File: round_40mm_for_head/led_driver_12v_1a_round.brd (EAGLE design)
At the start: 38 x 38 mm, 44 parts, among them IC1 LM2936MP-3.0, Q1 BSZ0902NSI, Q2 BSZ0902NSI, Q3 BSZ0902NSI, Q4 BSZ0902NSI, Q5 BSZ0902NSI, X1 87758-1016

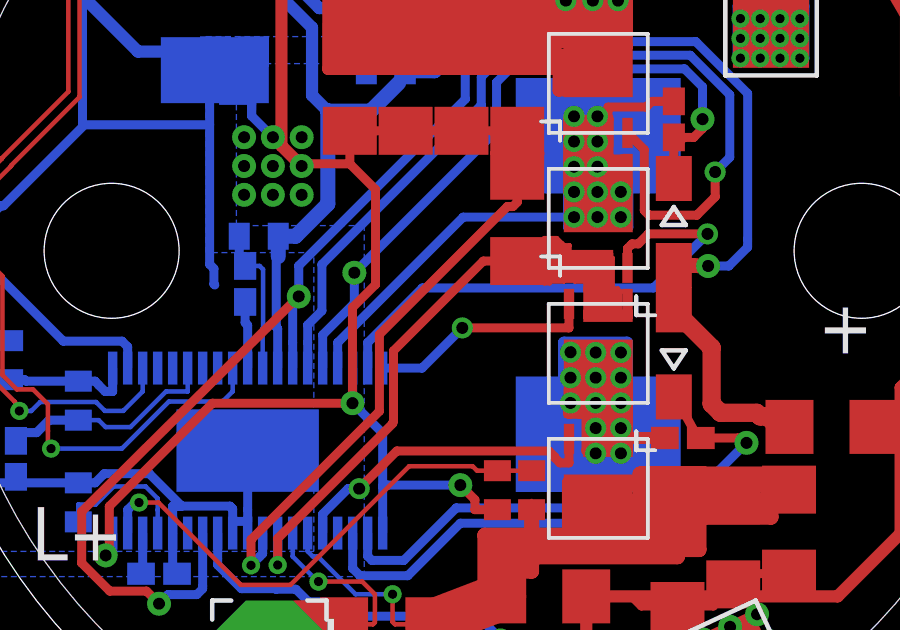
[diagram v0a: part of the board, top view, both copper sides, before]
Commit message: kevlin connection changed
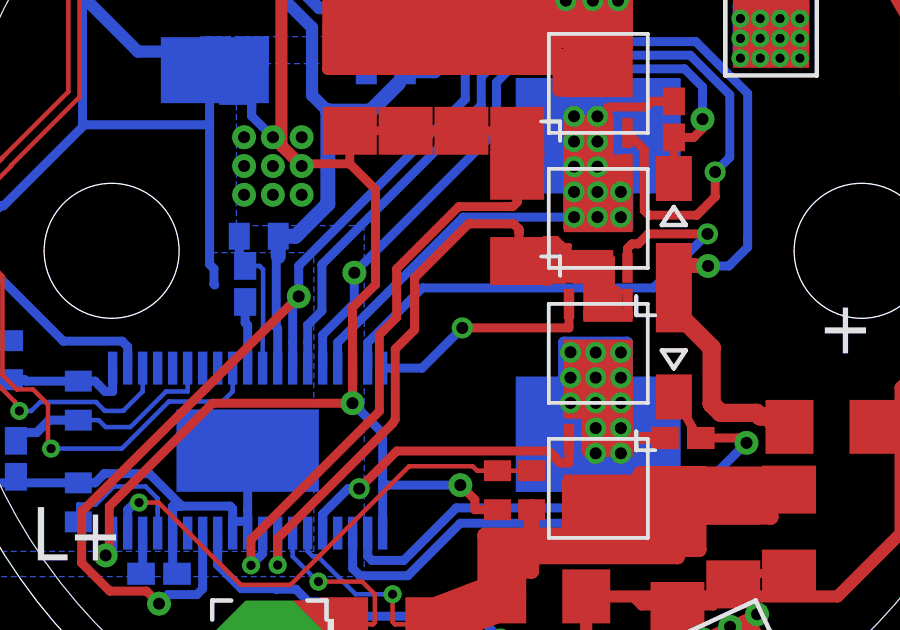
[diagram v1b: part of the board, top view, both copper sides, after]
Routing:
- net SNSP: track 58.4 -> 61.2 mm
- net SNSN: track 18.0 -> 19.0 mm
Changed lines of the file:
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@@
 <element name="PAD4" library="wirepad" package="5-2,5" value="LED+" x="25.08" y="3.78" smashed="yes" rot="R115"/>
 <element name="U$4" library="SparkFun-Passives" package="GND_CONNECT" value="GND_CONNECT" x="8.955" y="23.625" smashed="yes" rot="MR270"/>
-<element name="IC1" library="national-semiconductor" package="SOT223" value="LM2936MP-3.0" x="8.94" y="27.12" rot="MR180">
+<element name="IC1" library="national-semiconductor" package="SOT223" value="LM2936MP-3.0" x="8.94" y="27.12" smashed="yes" rot="MR180">
 <attribute name="OC_FARNELL" value="1496125" x="8.94" y="27.12" size="1.778" layer="28" rot="MR180" display="off"/>
 <attribute name="MF" value="NATIONAL SEMICONDUCTOR" x="8.94" y="27.12" size="1.778" layer="28" rot="MR180" display="off"/>
@@
 <wire x1="19.02" y1="19.62" x2="18.873390625" y2="19.473390625" width="0.3" layer="1"/>
 <wire x1="18.873390625" y1="19.473390625" x2="18.688" y2="19.473390625" width="0.3" layer="1"/>
-<wire x1="18.688" y1="19.473390625" x2="14.42515" y2="15.210540625" width="0.3" layer="1"/>
+<wire x1="18.688" y1="19.473390625" x2="17.073390625" y2="19.473390625" width="0.3" layer="1"/>
+<wire x1="17.073390625" y1="19.473390625" x2="15" y2="17.4" width="0.3" layer="1"/>
+<wire x1="15" y1="17.4" x2="15" y2="15.78" width="0.3" layer="1"/>
+<wire x1="15" y1="15.78" x2="14.52" y2="15.3" width="0.3" layer="1"/>
+<wire x1="14.52" y1="15.3" x2="14.42515" y2="15.210540625" width="0.3" layer="1"/>
 <wire x1="14.42515" y1="15.210540625" x2="14.42515" y2="12.65243125" width="0.3" layer="1"/>
 <wire x1="14.42515" y1="12.65243125" x2="10.146590625" y2="8.37386875" width="0.3" layer="1"/>
@@
 <contactref element="Q3" pad="S@3"/>
 <contactref element="R8" pad="2"/>
-<wire x1="19.02" y1="17.658" x2="17.889890625" y2="17.658" width="0.3" layer="1"/>
-<wire x1="17.889890625" y1="17.658" x2="14.89588125" y2="14.663990625" width="0.3" layer="1"/>
-<wire x1="14.89588125" y1="14.663990625" x2="14.89588125" y2="12.32296875" width="0.3" layer="1"/>
-<wire x1="14.89588125" y1="12.32296875" x2="14.879590625" y2="12.30668125" width="0.1524" layer="1"/>
-<wire x1="14.879590625" y1="12.30668125" x2="14.87223125" y2="12.24668125" width="0.3" layer="1"/>
+<wire x1="14.95588125" y1="14.723990625" x2="14.95588125" y2="12.38296875" width="0.3" layer="1"/>
+<wire x1="14.95588125" y1="12.38296875" x2="14.939590625" y2="12.36668125" width="0.1524" layer="1"/>
+<wire x1="14.939590625" y1="12.36668125" x2="14.87223125" y2="12.24668125" width="0.3" layer="1"/>
 <wire x1="14.87223125" y1="12.24668125" x2="11.035309375" y2="8.409759375" width="0.3" layer="1"/>
 <wire x1="11.035309375" y1="8.409759375" x2="11.035309375" y2="7.52523125" width="0.3" layer="1"/>
@@
 <via x="11.035309375" y="7.52523125" extent="1-16" drill="0.3048" diameter="0.6096"/>
 <wire x1="21.395" y1="17.43" x2="21.395" y2="16.701390625" width="0.1524" layer="1"/>
+<wire x1="19.02" y1="17.658" x2="19.08" y2="17.658" width="0.4064" layer="1"/>
+<wire x1="19.08" y1="17.658" x2="19.08" y2="18.6" width="0.3048" layer="1"/>
+<wire x1="19.08" y1="18.6" x2="19.08" y2="18.72" width="0.3048" layer="1"/>
+<wire x1="19.08" y1="18.72" x2="18.9" y2="18.9" width="0.3048" layer="1"/>
+<wire x1="18.9" y1="18.9" x2="17.4" y2="18.9" width="0.3048" layer="1"/>
+<wire x1="17.4" y1="18.9" x2="15.6" y2="17.1" width="0.3048" layer="1"/>
+<wire x1="15.6" y1="17.1" x2="15.6" y2="15.368109375" width="0.3048" layer="1"/>
+<wire x1="15.6" y1="15.368109375" x2="14.95588125" y2="14.723990625" width="0.3048" layer="1"/>
 </signal>
 <signal name="ISN">

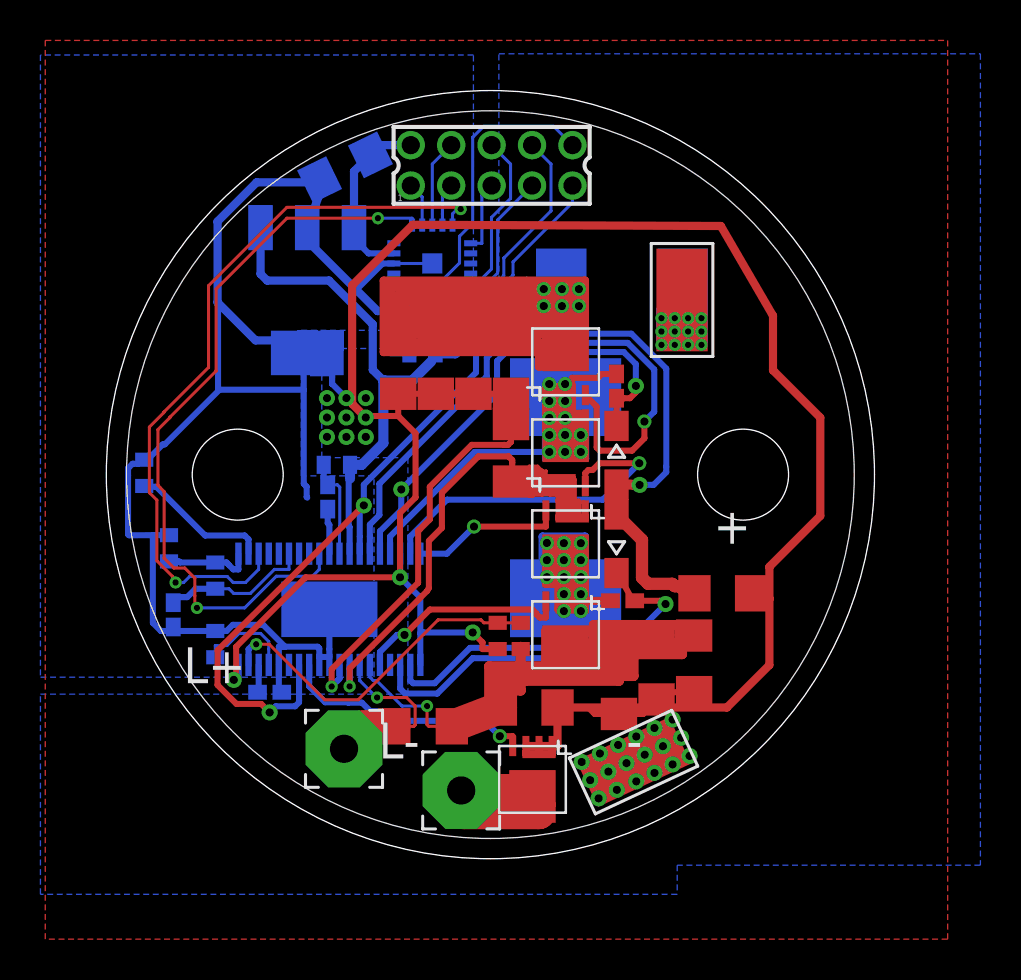
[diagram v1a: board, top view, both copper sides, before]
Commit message: added adc resistors shutdown
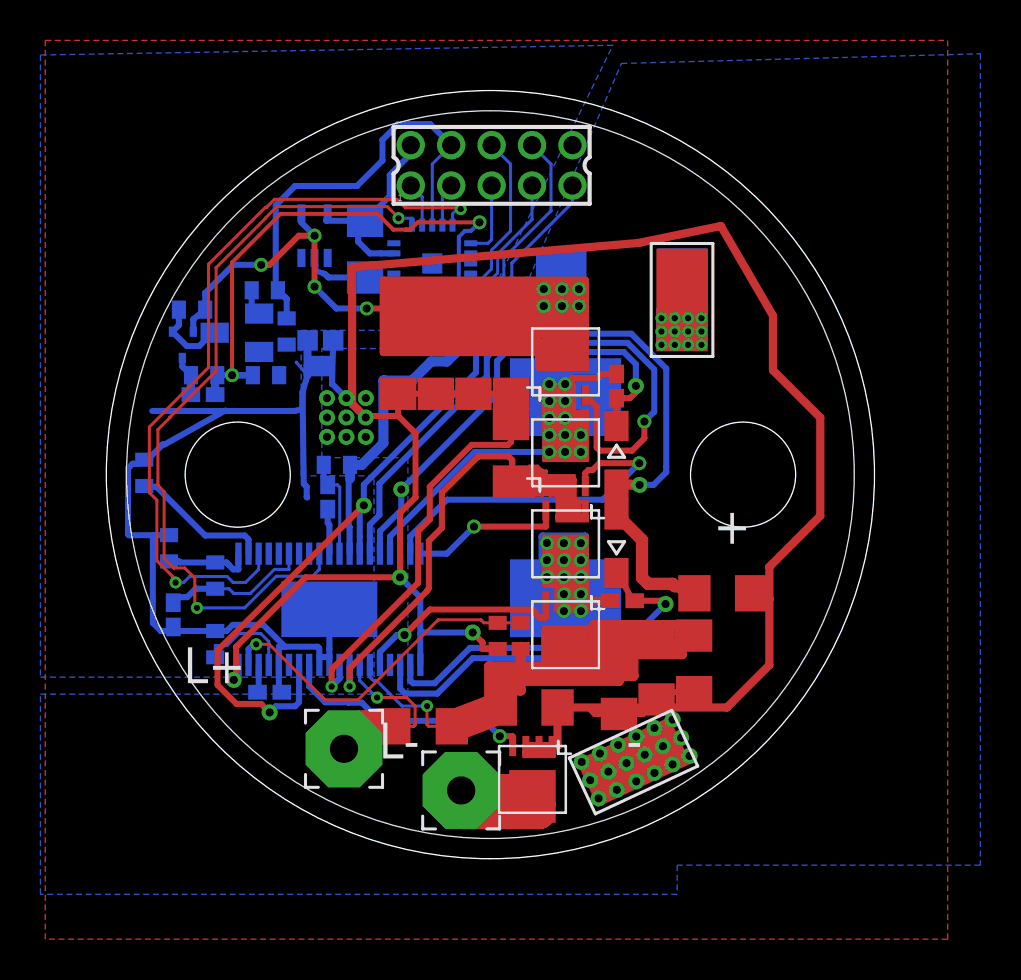
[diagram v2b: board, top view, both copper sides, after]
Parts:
- removed IC1: LM2936MP-3.0, national-semiconductor:SOT223
- added C17: 100nF, resistor:C0402K
- added R12, R3: 10k, resistor:R0402
- added R13: 10Meg, resistor:R0402
- added T1: BCW-60B, transistor-neu-to92:SOT23-BEC
- added U$3: TPS71550, TPS715:SC70
- added U$5: SI1013, Si1013:SOT-416
- C16: value 10uF -> 4.7uF
- R11: value 50m (Ohmite MCS1632R005FER) -> 5m (Ohmite MCS1632R005FER)
- R5: value 100k -> 110k
- R6: value 56.9k -> 10k
- R8: value 10m (Riedon CSR1206-0R001F1) -> 1m (Riedon CSR1206-0R001F1)
- moved R5 10.9 mm to (3.84, 22.9), turned to 180 degrees
- moved R6 6.62 mm to (6.90, 22.9), turned to 180 degrees
- moved C16 4.17 mm to (11.8, 29.2), turned to 270 degrees
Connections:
- net N$11 renamed PA2
- net N$13 renamed PA3
- net N$16 renamed SCL
- net N$17 renamed MISO
- net N$18 renamed MOSI
- net N$20 renamed PB1
- net N$23 renamed PB2
- removed net N$22: U$2.13, X1.4
- removed net N$8: U$2.4, X1.10
- new net N$24: R12.2, T1.B
- new net N$25: R3.2, T1.C, U$5.1
- new net N$27: C17.2, R5.1, U$5.3
- new net RESET: R12.1, R13.2, U$2.13, X1.4
- net +12V: now also R3.1, U$3.4, U$5.2; no longer IC1.1, R5.1
- net DGND: now also R13.1, T1.E, U$3.2, X1.10; no longer IC1.2, IC1.4
- net N$12: now also U$3.5; no longer IC1.3
- net N$15: now also C17.1
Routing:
- net N$15: track 4.33 -> 30.7 mm, vias 0 -> 2
- net DGND: track 80.3 -> 57.0 mm
- net RESET: track 0.00 -> 22.2 mm
- net N$8: track 15.0 -> 0.00 mm
- net +12V: track 178.2 -> 184.0 mm, vias 6 -> 10
- net N$22: track 4.34 -> 0.00 mm
- net N$25: track 0.00 -> 3.88 mm
- net N$27: track 0.00 -> 2.00 mm
- net N$12: track 8.95 -> 10.3 mm
- net N$24: track 0.00 -> 1.30 mm
- net N$14: track 37.0 -> 38.0 mm
- net N$10: track 37.5 -> 38.3 mm

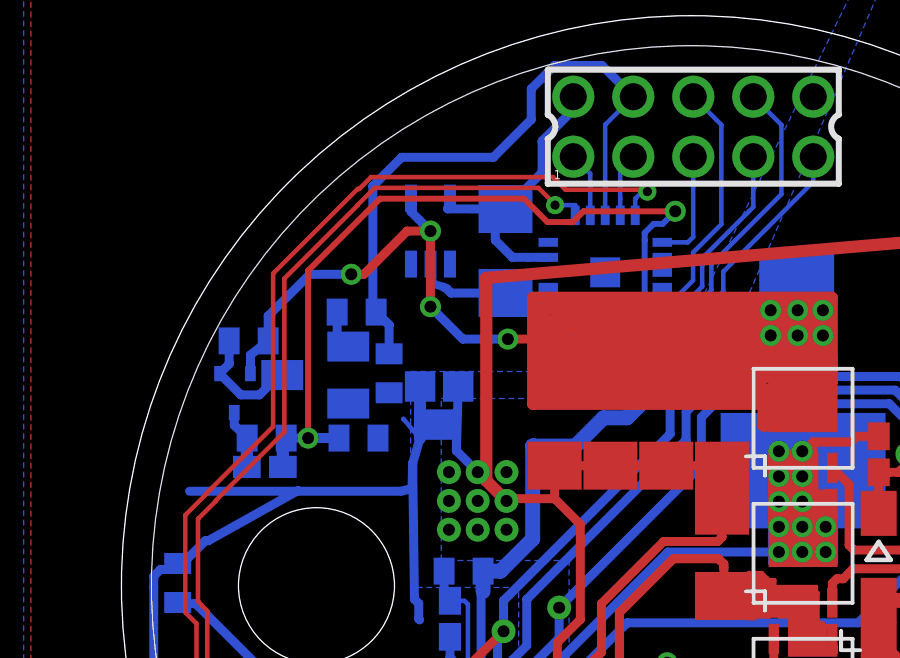
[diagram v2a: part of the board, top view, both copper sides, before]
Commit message: added resistor to adc
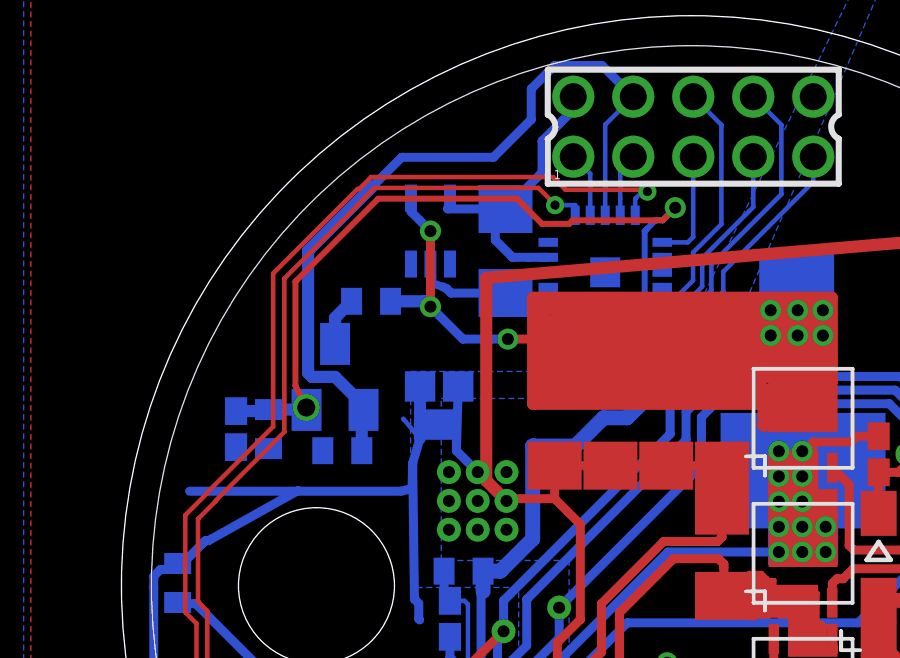
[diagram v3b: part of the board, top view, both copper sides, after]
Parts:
- removed R12, R3, R6: 10k, resistor:R0402
- removed R13: 10Meg, resistor:R0402
- removed R5: 110k, resistor:R0402
- removed T1: BCW-60B, transistor-neu-to92:SOT23-BEC
- removed U$5: SI1013, Si1013:SOT-416
- added Q7: BSS123, transistor-small-signal:SOT23
- added R1: 10k, resistor:R0402
- added R16: 10Meg, resistor:R0402
- added R2: 110k, resistor:R0402
- C17: value 100nF -> 0.1uF
- moved C17 1.58 mm to (2.82, 23.2), turned to 270 degrees
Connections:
- removed net N$24: R12.2, T1.B
- removed net N$25: R3.2, T1.C, U$5.1
- removed net N$27: C17.2, R5.1, U$5.3
- new net N$8: Q7.3, R2.2
- net +12V: now also R2.1; no longer R3.1, U$5.2
- net DGND: now also C17.2, R1.2, R16.2; no longer R13.1, R6.2, T1.E
- net N$15: now also Q7.2, R1.1; no longer R5.2, R6.1
- net RESET: now also Q7.1, R16.1; no longer R12.1, R13.2
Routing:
- net +12V: track 184.0 -> 176.7 mm, vias 10 -> 9
- net RESET: track 22.2 -> 26.7 mm
- net N$25: track 3.88 -> 0.00 mm
- net N$15: track 30.7 -> 27.9 mm
- net N$27: track 2.00 -> 0.00 mm
- net N$8: track 0.00 -> 1.65 mm
- net N$24: track 1.30 -> 0.00 mm

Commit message: moved components inside
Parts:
- moved C1 1.20 mm to (2.08, 18.0)
- moved C5 0.95 mm to (3.21, 11.4)
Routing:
- net DGND: track 57.0 -> 59.2 mm
- net N$4: track 6.97 -> 6.17 mm
- net N$1: track 7.38 -> 6.79 mm
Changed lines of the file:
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@@
 <element name="C6" library="resistor" package="C0402K" value="0.1uF" x="24.24" y="22.38" smashed="yes" rot="R90"/>
 <element name="C7" library="resistor" package="C0402K" value="0.1uF" x="24.54" y="11.76" smashed="yes" rot="R180"/>
-<element name="C5" library="resistor" package="C0402K" value="0.1uF" x="2.31" y="11.065" smashed="yes" rot="MR270"/>
-<element name="C1" library="resistor" package="C0402" value="22nF" x="0.875" y="18.09" smashed="yes" rot="MR270"/>
+<element name="C5" library="resistor" package="C0402K" value="0.1uF" x="3.21" y="11.365" smashed="yes" rot="MR270"/>
+<element name="C1" library="resistor" package="C0402" value="22nF" x="2.075" y="18.03" smashed="yes" rot="MR270"/>
 <element name="C2" library="resistor" package="C0402K" value="22nF" x="7.08" y="7.235" smashed="yes" rot="MR180"/>
 <element name="C3" library="resistor" package="C0402K" value="470nF" x="9.95" y="16.895" smashed="yes" rot="MR90"/>
@@
 <wire x1="4.39" y1="12.355" x2="3.415" y2="12.355" width="0.3048" layer="16"/>
 <wire x1="3.415" y1="12.355" x2="3" y2="11.94" width="0.3048" layer="16"/>
-<wire x1="3" y1="11.94" x2="2.585" y2="11.94" width="0.3048" layer="16"/>
-<wire x1="2.585" y1="11.94" x2="2.31" y2="11.665" width="0.3048" layer="16"/>
+<wire x1="3" y1="11.94" x2="3.185" y2="11.94" width="0.3048" layer="16"/>
+<wire x1="3.185" y1="11.94" x2="3.21" y2="11.965" width="0.3048" layer="16"/>
 </signal>
 <signal name="GND" class="1">
@@
 <contactref element="U$1" pad="P$2"/>
 <contactref element="C1" pad="2"/>
-<wire x1="0.875" y1="17.44" x2="0.96" y2="17.46" width="0.3" layer="16"/>
-<wire x1="0.96" y1="17.46" x2="1.018609375" y2="17.401390625" width="0.3" layer="16"/>
-<wire x1="1.018609375" y1="17.401390625" x2="1.475" y2="17.401390625" width="0.3" layer="16"/>
+<wire x1="2.075" y1="17.38" x2="2.04" y2="17.34" width="0.3" layer="16"/>
+<wire x1="2.04" y1="17.34" x2="1.918609375" y2="17.161390625" width="0.3" layer="16"/>
+<wire x1="1.918609375" y1="17.161390625" x2="2.015" y2="16.861390625" width="0.3" layer="16"/>
 <wire x1="6.035" y1="14.09" x2="6.035" y2="14.799346875" width="0.3" layer="16"/>
 <wire x1="6.035" y1="14.799346875" x2="5.8457375" y2="14.988609375" width="0.3" layer="16"/>
 <wire x1="5.8457375" y1="14.988609375" x2="3.88778125" y2="14.988609375" width="0.3" layer="16"/>
-<wire x1="3.88778125" y1="14.988609375" x2="1.475" y2="17.401390625" width="0.3" layer="16"/>
+<wire x1="3.88778125" y1="14.988609375" x2="2.015" y2="16.861390625" width="0.3" layer="16"/>
 </signal>
 <signal name="N$5">
@@
 <wire x1="0.3" y1="18.54" x2="0.6" y2="18.54" width="0.3" layer="16"/>
 <wire x1="0.6" y1="18.54" x2="0.588159375" y2="18.581390625" width="0.3" layer="16"/>
-<wire x1="0.875" y1="18.74" x2="0.815" y2="18.685015625" width="0.3" layer="16"/>
+<wire x1="2.075" y1="18.68" x2="0.815" y2="18.685015625" width="0.3" layer="16"/>
 <wire x1="0.815" y1="18.685015625" x2="0.771375" y2="18.641390625" width="0.3" layer="16"/>
 <wire x1="0.771375" y1="18.641390625" x2="0.588159375" y2="18.581390625" width="0.3" layer="16"/>
@@
 <wire x1="1.7001" y1="10.265" x2="1.301390625" y2="10.663709375" width="0.3" layer="16"/>
 <wire x1="1.301390625" y1="10.663709375" x2="1.301390625" y2="15.005" width="0.3" layer="16"/>
-<wire x1="0.875" y1="18.74" x2="0.96" y2="18.66" width="0.3" layer="16"/>
+<wire x1="2.075" y1="18.68" x2="0.96" y2="18.66" width="0.3" layer="16"/>
 <wire x1="0.96" y1="18.66" x2="1.798609375" y2="19.498609375" width="0.3" layer="16"/>
 <wire x1="1.798609375" y1="19.498609375" x2="1.895" y2="19.498609375" width="0.3" layer="16"/>
@@
 <wire x1="1.86" y1="13.86" x2="2.34" y2="13.38" width="0.1524" layer="1"/>
 <wire x1="2.34" y1="13.38" x2="2.88" y2="13.38" width="0.1524" layer="1"/>
-<wire x1="2.88" y1="13.38" x2="3.37795" y2="12.88205" width="0.1524" layer="1"/>
-<wire x1="3.37795" y1="12.88205" x2="3.37795" y2="11.99783125" width="0.1524" layer="1"/>
-<wire x1="3.37795" y1="11.99783125" x2="3.37795" y2="11.54298125" width="0.1524" layer="1"/>
-<wire x1="3.37795" y1="11.54298125" x2="3.48175" y2="11.40678125" width="0.1524" layer="1"/>
+<wire x1="2.88" y1="13.38" x2="3.61795" y2="12.64205" width="0.1524" layer="1"/>
+<wire x1="3.61795" y1="12.64205" x2="3.61795" y2="11.72298125" width="0.1524" layer="1"/>
+<wire x1="3.61795" y1="11.72298125" x2="3.61795" y2="11.75783125" width="0.1524" layer="1"/>
+<wire x1="3.61795" y1="11.75783125" x2="3.61795" y2="11.72298125" width="0.1524" layer="1"/>
+<wire x1="3.61795" y1="11.72298125" x2="4.02175" y2="11.34678125" width="0.1524" layer="1"/>
 <wire x1="14.125" y1="30.68573125" x2="13.454490625" y2="30.68573125" width="0.1524" layer="16"/>
 <wire x1="13.454490625" y1="30.68573125" x2="13.45411875" y2="30.6861" width="0.1524" layer="16"/>
 <via x="13.45411875" y="30.6861" extent="1-16" drill="0.3048" diameter="0.6096"/>
 <wire x1="14.125" y1="30.345" x2="14.125" y2="30.68573125" width="0.1524" layer="16"/>
-<wire x1="3.48175" y1="11.40678125" x2="5.84101875" y2="11.40678125" width="0.1524" layer="16"/>
+<wire x1="4.02175" y1="11.34678125" x2="5.84101875" y2="11.40678125" width="0.1524" layer="16"/>
 <wire x1="5.84101875" y1="11.40678125" x2="7.409340625" y2="12.9751" width="0.1524" layer="16"/>
 <wire x1="7.409340625" y1="12.9751" x2="9.198709375" y2="12.9751" width="0.1524" layer="16"/>
 <wire x1="9.198709375" y1="12.9751" x2="9.535" y2="13.311390625" width="0.1524" layer="16"/>
-<via x="3.48175" y="11.40678125" extent="1-16" drill="0.3048" diameter="0.6096"/>
+<via x="4.02175" y="11.34678125" extent="1-16" drill="0.3048" diameter="0.6096"/>
 <wire x1="9.535" y1="14.09" x2="9.535" y2="13.311390625" width="0.1524" layer="16"/>
 </signal>
